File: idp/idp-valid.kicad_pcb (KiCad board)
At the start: 2 copper layers, 302.3 x 247 mm, 307 parts, among them J1 PinHeader_2x17_P2.54mm_Vertic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, J2 PinHeader_2x32_P2.54mm_Vertic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, J3 PinHeader_1x03_P2.54mm_Vertic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, J4 PinHeader_2x25_P2.54mm_Vertic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, J5 PinHeader_1x05_P2.54mm_Vertic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, J6 PinHeader_2x20_P2.54mm_Vertic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, J7 PinHeader_2x13_P2.54mm_Vertic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, J8 PinHeader_2x13_P2.54mm_Vertic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, J9 PinHeader_2x13_P2.54mm_Vertic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, X10 Partner_Molex_Mega-Fit_76829-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, Y1 8.000, Y2 32.768 kHZ, Y3 1.8432

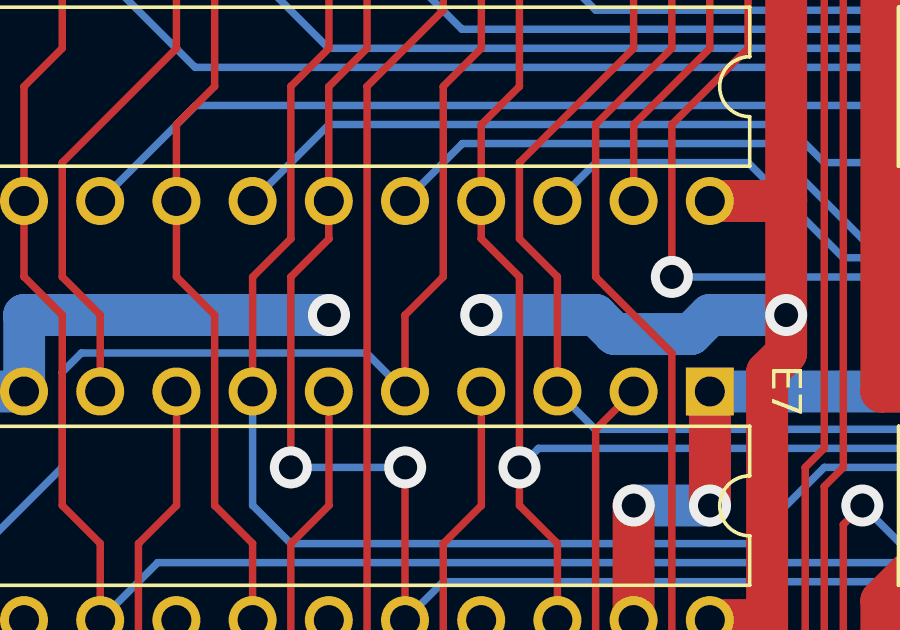
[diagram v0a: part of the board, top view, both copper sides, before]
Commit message: Adds missing CX
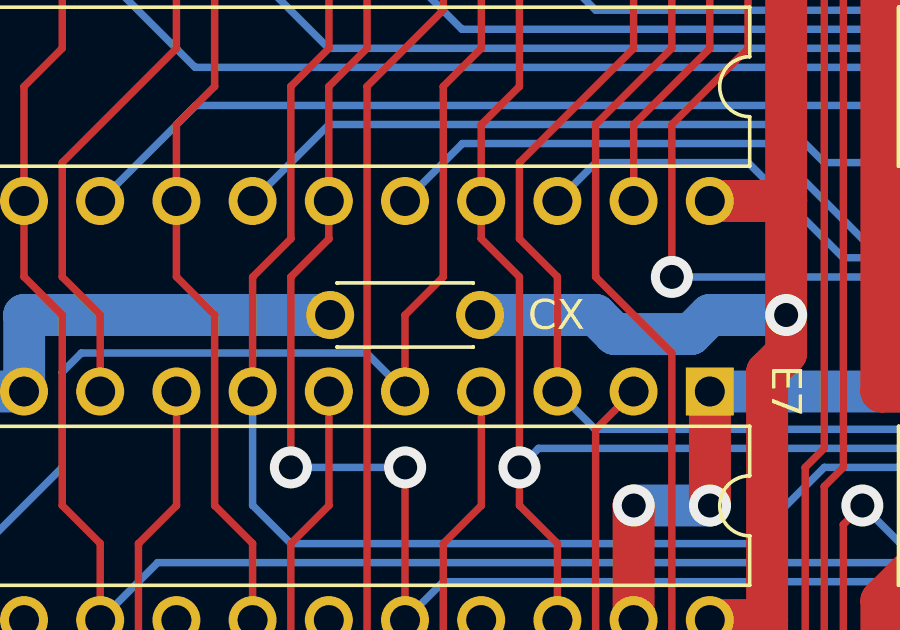
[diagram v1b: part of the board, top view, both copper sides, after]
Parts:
- added CX: 104, Capacitor_THT:C_Disc_D4.3mm_W1.9mm_P5.00mm, F.Cu at (82.5, 130.8)
- renumbered REF** to BAT
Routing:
- net (no net): vias 1039 -> 1037
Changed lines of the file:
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@@
     )
   )
+  (footprint "Capacitor_THT:C_Disc_D4.3mm_W1.9mm_P5.00mm" (layer "F.Cu")
+    (at 82.51 130.81 180)
+    (descr "C, Disc series, Radial, pin pitch=5.00mm, , diameter*width=4.3*1.9mm^2, Capacitor, http://www.vishay.com/docs/45233/krseries.pdf")
+    (tags "C Disc series Radial pin pitch 5.00mm  diameter 4.3mm width 1.9mm Capacitor")
+    (attr through_hole)
+    (fp_text reference "CX" (at -2.54 0 unlocked) (layer "F.SilkS")
+        (effects (font (size 1 1) (thickness 0.15)))
+    )
+    (fp_text value "104" (at 2.5 0 unlocked) (layer "F.Fab")
+        (effects (font (size 1 1) (thickness 0.15)))
+    )
+    (fp_text user "${REFERENCE}" (at 2.5 0) (layer "F.Fab") hide
+        (effects (font (size 0.86 0.86) (thickness 0.129)))
+    )
+    (fp_line (start 0.23 -1.07) (end 0.23 -1.055)
+      (stroke (width 0.12) (type solid)) (layer "F.SilkS"))
+    (fp_line (start 0.23 -1.07) (end 4.77 -1.07)
+      (stroke (width 0.12) (type solid)) (layer "F.SilkS"))
+    (fp_line (start 0.23 1.055) (end 0.23 1.07)
+      (stroke (width 0.12) (type solid)) (layer "F.SilkS"))
+    (fp_line (start 0.23 1.07) (end 4.77 1.07)
+      (stroke (width 0.12) (type solid)) (layer "F.SilkS"))
+    (fp_line (start 4.77 -1.07) (end 4.77 -1.055)
+      (stroke (width 0.12) (type solid)) (layer "F.SilkS"))
+    (fp_line (start 4.77 1.055) (end 4.77 1.07)
+      (stroke (width 0.12) (type solid)) (layer "F.SilkS"))
+    (fp_line (start -1.05 -1.2) (end -1.05 1.2)
+      (stroke (width 0.05) (type solid)) (layer "F.CrtYd"))
+    (fp_line (start -1.05 1.2) (end 6.05 1.2)
+      (stroke (width 0.05) (type solid)) (layer "F.CrtYd"))
+    (fp_line (start 6.05 -1.2) (end -1.05 -1.2)
+      (stroke (width 0.05) (type solid)) (layer "F.CrtYd"))
+    (fp_line (start 6.05 1.2) (end 6.05 -1.2)
+      (stroke (width 0.05) (type solid)) (layer "F.CrtYd"))
+    (fp_line (start 0.35 -0.95) (end 0.35 0.95)
+      (stroke (width 0.1) (type solid)) (layer "F.Fab"))
+    (fp_line (start 0.35 0.95) (end 4.65 0.95)
+      (stroke (width 0.1) (type solid)) (layer "F.Fab"))
+    (fp_line (start 4.65 -0.95) (end 0.35 -0.95)
+      (stroke (width 0.1) (type solid)) (layer "F.Fab"))
+    (fp_line (start 4.65 0.95) (end 4.65 -0.95)
+      (stroke (width 0.1) (type solid)) (layer "F.Fab"))
+    (pad "1" thru_hole circle (at 0 0 180) (size 1.6 1.6) (drill 1) (layers "*.Cu" "*.Mask")
+      (solder_mask_margin 0.2) (clearance 0.2))
+    (pad "2" thru_hole circle (at 5 0 180) (size 1.6 1.6) (drill 1) (layers "*.Cu" "*.Mask")
+      (solder_mask_margin 0.2) (clearance 0.2))
+    (model "${KICAD6_3DMODEL_DIR}/Capacitor_THT.3dshapes/C_Disc_D4.3mm_W1.9mm_P5.00mm.wrl"
+      (offset (xyz 0 0 0))
+      (scale (xyz 1 1 1))
+      (rotate (xyz 0 0 0))
+    )
+  )
   (footprint "Resistor_THT:R_Axial_DIN0207_L6.3mm_D2.5mm_P7.62mm_Horizontal" (layer "F.Cu")
     (at 245.11 129.54 90)
@@
     (tags "connector Molex Mega-Fit side entry")
     (attr through_hole)
-    (fp_text reference "REF**" (at -0.65 -0.7) (layer "F.SilkS") hide
+    (fp_text reference "BAT" (at -0.65 -0.7) (layer "F.SilkS") hide
         (effects (font (size 1 1) (thickness 0.15)))
     )
@@
   (via (at 254 273.685) (size 1.4) (drill 0.8) (layers "F.Cu" "B.Cu") (net 0))
   (via (at 220.98 227.33) (size 1.4) (drill 0.8) (layers "F.Cu" "B.Cu") (net 0))
-  (via (at 77.47 130.81) (size 1.4) (drill 0.8) (layers "F.Cu" "B.Cu") (net 0))
   (via (at 283.21 175.26) (size 1.4) (drill 0.8) (layers "F.Cu" "B.Cu") (net 0))
   (via (at 74.93 180.34) (size 1.4) (drill 0.8) (layers "F.Cu" "B.Cu") (net 0))
@@
   (via (at 97.79 193.04) (size 1.4) (drill 0.8) (layers "F.Cu" "B.Cu") (net 0))
   (via (at 114.3 192.405) (size 1.4) (drill 0.8) (layers "F.Cu" "B.Cu") (net 0))
-  (via (at 82.55 130.81) (size 1.4) (drill 0.8) (layers "F.Cu" "B.Cu") (net 0))
   (via (at 173.99 170.18) (size 1.4) (drill 0.8) (layers "F.Cu" "B.Cu") (net 0))
   (via (at 297.18 172.72) (size 1.4) (drill 0.8) (layers "F.Cu" "B.Cu") (net 0))

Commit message: Adds missing traces (visual validation)
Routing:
- net (no net): track 72537.9 -> 72770.4 mm, vias 1037 -> 1038
